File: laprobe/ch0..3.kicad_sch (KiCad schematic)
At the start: 69 parts, among them U201 LMH7324

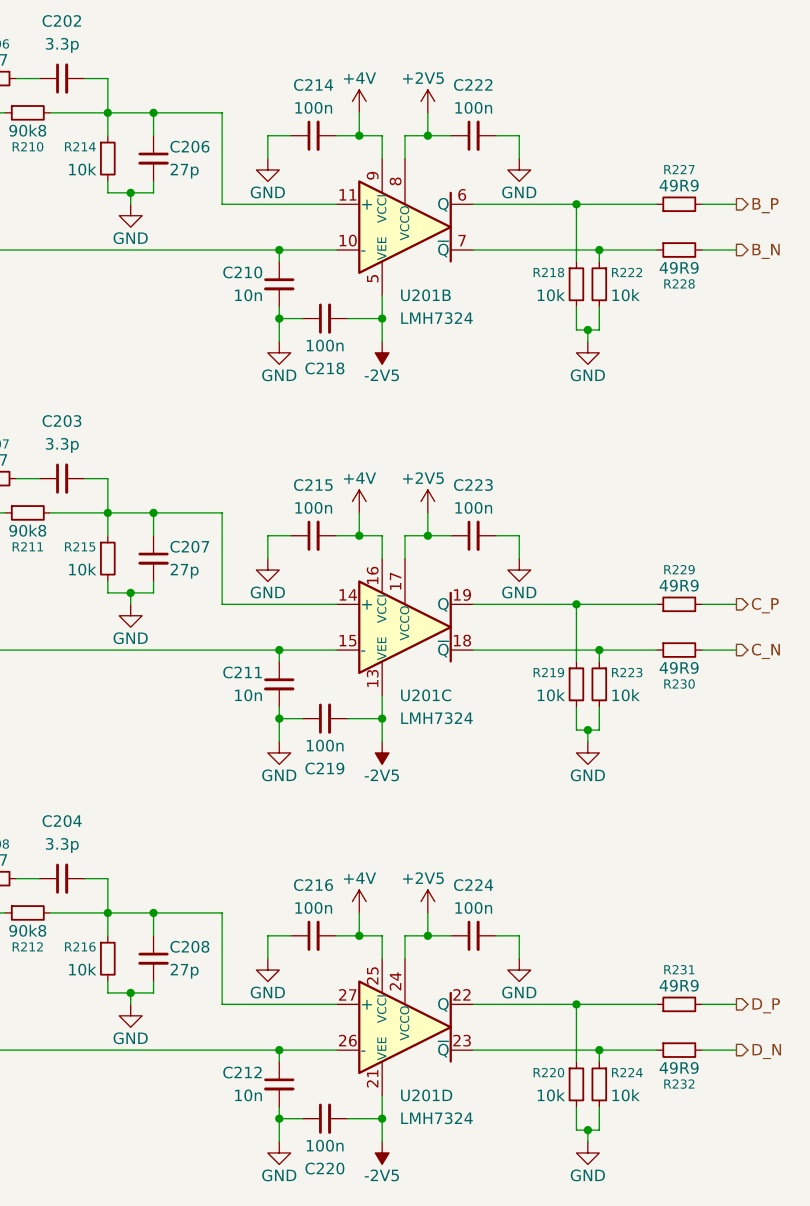
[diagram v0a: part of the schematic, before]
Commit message: Switch around some channels on buffer/tranceiver for routing
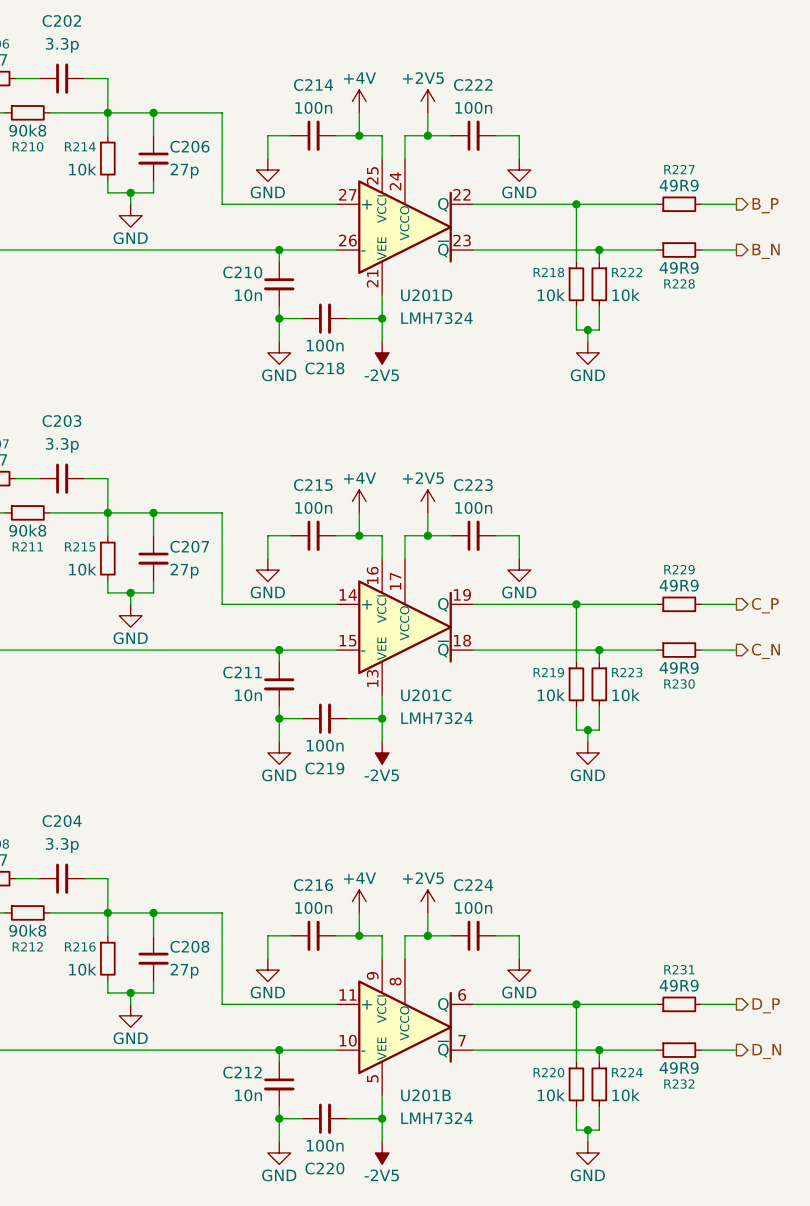
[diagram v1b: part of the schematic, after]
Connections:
- net at C204.2, C208.1, R212.2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: now also U201.11 (+); no longer U201.27 (+)
- net at R218.1, R227.1: now also U201.22 (Q); no longer U201.6 (Q)
- net at R220.1, R231.1: now also U201.6 (Q); no longer U201.22 (Q)
- net at R224.1, R232.1: now also U201.7 (~{Q}); no longer U201.23 (~{Q})
- net at C202.2, C206.1, R210.2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: now also U201.27 (+); no longer U201.11 (+)
- net at R222.1, R228.1: now also U201.23 (~{Q}); no longer U201.7 (~{Q})
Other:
- moved on the sheet: U201B, U201D
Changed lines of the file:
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@@
 	(symbol
 		(lib_id "Comparator:LMH7324")
-		(at 102.87 175.26 0)
+		(at 102.87 86.36 0)
 		(unit 4)
 		(exclude_from_sim no)
@@
 		(fields_autoplaced yes)
 		(property "Reference" "U201"
-			(at 102.2811 182.88 0)
+			(at 102.2811 93.98 0)
 			(effects
 				(font
@@
 		)
 		(property "Value" "LMH7324"
-			(at 102.2811 185.42 0)
+			(at 102.2811 96.52 0)
 			(effects
 				(font
@@
 		)
 		(property "Footprint" "Package_DFN_QFN:WQFN-32-1EP_5x5mm_P0.5mm_EP3.1x3.1mm"
-			(at 101.6 191.77 0)
+			(at 101.6 102.87 0)
 			(effects
 				(font
@@
 		)
 		(property "Datasheet" "http://www.ti.com/lit/ds/symlink/lmh7324.pdf"
-			(at 102.87 175.26 0)
+			(at 102.87 86.36 0)
 			(effects
 				(font
@@
 		)
 		(property "Description" "Quad 700 ps High Speed Comparator with RSPECL Outputs, WQFN-32"
-			(at 102.87 175.26 0)
+			(at 102.87 86.36 0)
 			(effects
 				(font
@@
 	(symbol
 		(lib_id "Comparator:LMH7324")
-		(at 102.87 86.36 0)
+		(at 102.87 175.26 0)
 		(unit 2)
 		(exclude_from_sim no)
@@
 		(fields_autoplaced yes)
 		(property "Reference" "U201"
-			(at 102.2811 93.98 0)
+			(at 102.2811 182.88 0)
 			(effects
 				(font
@@
 		)
 		(property "Value" "LMH7324"
-			(at 102.2811 96.52 0)
+			(at 102.2811 185.42 0)
 			(effects
 				(font
@@
 		)
 		(property "Footprint" "Package_DFN_QFN:WQFN-32-1EP_5x5mm_P0.5mm_EP3.1x3.1mm"
-			(at 101.6 102.87 0)
+			(at 101.6 191.77 0)
 			(effects
 				(font
@@
 		)
 		(property "Datasheet" "http://www.ti.com/lit/ds/symlink/lmh7324.pdf"
-			(at 102.87 86.36 0)
+			(at 102.87 175.26 0)
 			(effects
 				(font
@@
 		)
 		(property "Description" "Quad 700 ps High Speed Comparator with RSPECL Outputs, WQFN-32"
-			(at 102.87 86.36 0)
+			(at 102.87 175.26 0)
 			(effects
 				(font
